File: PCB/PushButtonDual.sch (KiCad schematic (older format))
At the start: 3 parts, among them SW3 PCB_Push_Button, SW4 PCB_Push_Button

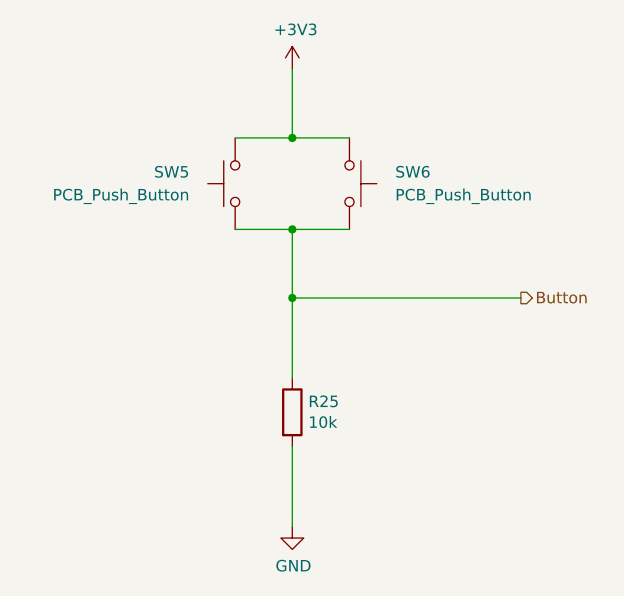
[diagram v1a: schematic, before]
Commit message: Improve the push buttons
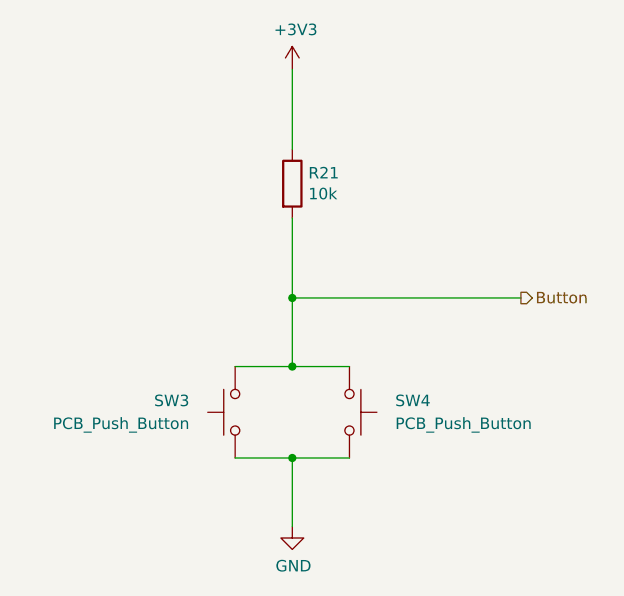
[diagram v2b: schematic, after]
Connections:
- net +3V3: now also R21.1; no longer SW3.1, SW4.1
- net Button: now also R21.2, SW3.1, SW4.1; no longer R21.1, SW3.2, SW4.2
- net GND: now also SW3.2, SW4.2; no longer R21.2
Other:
- moved on the sheet: R21, SW3, SW4
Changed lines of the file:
@@
 $Descr A4 11693 8268
 encoding utf-8
-Sheet 13 19
+Sheet 11 19
 Title "Litter Robot 3 - Push button (dual)"
 Date "2021-03-28"
@@
 L Device:R R?
 U 1 1 604E1842
-P 5000 4000
+P 5000 3000
 AR Path="/603F20AB/604E1842" Ref="R?"  Part="1"
 AR Path="/603F1DCE/604E1842" Ref="R?"  Part="1"
@@
 AR Path="/603F1F4D/605BE155/604E1842" Ref="R?"  Part="1"
 AR Path="/603F1F4D/605BE15D/604E1842" Ref="R?"  Part="1"
-F 0 "R25" H 5070 4046 50  0000 L CNN
-F 1 "10k" H 5070 3955 50  0000 L CNN
-F 2 "Resistor_SMD:R_0603_1608Metric" V 4930 4000 50  0001 C CNN
-F 3 "https://www.bourns.com/docs/product-datasheets/CRxxxxx.pdf" H 5000 4000 50  0001 C CNN
-F 4 "CR0603-FX-1002ELF" H 5000 4000 50  0001 C CNN "Part_number"
-	1    5000 4000
+F 0 "R21" H 5070 3046 50  0000 L CNN
+F 1 "10k" H 5070 2955 50  0000 L CNN
+F 2 "Resistor_SMD:R_0603_1608Metric" V 4930 3000 50  0001 C CNN
+F 3 "https://www.bourns.com/docs/product-datasheets/CRxxxxx.pdf" H 5000 3000 50  0001 C CNN
+F 4 "CR0603-FX-1002ELF" H 5000 3000 50  0001 C CNN "Part_number"
+	1    5000 3000
 	1    0    0    -1
 $EndComp
@@
 AR Path="/603F1F4D/605BE155/604E1848" Ref="#PWR?"  Part="1"
 AR Path="/603F1F4D/605BE15D/604E1848" Ref="#PWR?"  Part="1"
-F 0 "#PWR046" H 5000 2350 50  0001 C CNN
+F 0 "#PWR040" H 5000 2350 50  0001 C CNN
 F 1 "+3V3" H 5015 2673 50  0000 C CNN
 F 2 "" H 5000 2500 50  0001 C CNN
@@
 AR Path="/603F1F4D/605BE155/604E184E" Ref="#PWR?"  Part="1"
 AR Path="/603F1F4D/605BE15D/604E184E" Ref="#PWR?"  Part="1"
-F 0 "#PWR047" H 5000 4250 50  0001 C CNN
+F 0 "#PWR041" H 5000 4250 50  0001 C CNN
 F 1 "GND" H 5005 4327 50  0000 C CNN
 F 2 "" H 5000 4500 50  0001 C CNN
@@
 $EndComp
 Wire Wire Line
-	5000 2500 5000 2800
+	5000 3500 5000 3800
 Wire Wire Line
-	5000 3200 5000 3500
-Wire Wire Line
-	5000 4150 5000 4500
+	5000 4200 5000 4500
 Wire Wire Line
 	6000 3500 5000 3500
-Connection ~ 5000 3500
-Wire Wire Line
-	5000 3500 5000 3850
 Text HLabel 6000 3500 2    50   Output ~ 0
 Button
 Wire Wire Line
-	4750 2800 5000 2800
-Connection ~ 5000 2800
+	4750 3800 5000 3800
+Connection ~ 5000 3800
 Wire Wire Line
-	5000 2800 5250 2800
+	5000 3800 5250 3800
 Wire Wire Line
-	4750 3200 5000 3200
-Connection ~ 5000 3200
+	4750 4200 5000 4200
+Connection ~ 5000 4200
 Wire Wire Line
-	5000 3200 5250 3200
+	5000 4200 5250 4200
 $Comp
 L Switch:SW_Push SW?
 U 1 1 604E185B
-P 5250 3000
+P 5250 4000
 AR Path="/603E03AA/603C09F0/604E185B" Ref="SW?"  Part="1"
 AR Path="/603E03AA/603C05C6/604E185B" Ref="SW?"  Part="1"
@@
 AR Path="/603F1F4D/605BE155/604E185B" Ref="SW?"  Part="1"
 AR Path="/603F1F4D/605BE15D/604E185B" Ref="SW?"  Part="1"
-F 0 "SW6" V 5200 3200 50  0000 L CNN
-F 1 "PCB_Push_Button" V 5300 3200 50  0000 L CNN
-F 2 "LitterRobot:PCB_Push_Button_5mm_0.4mm" H 5250 3200 50  0001 C CNN
-F 3 "~" H 5250 3200 50  0001 C CNN
-	1    5250 3000
+F 0 "SW4" V 5200 4200 50  0000 L CNN
+F 1 "PCB_Push_Button" V 5300 4200 50  0000 L CNN
+F 2 "LitterRobot:PCB_Push_Button_5mm_0.4mm" H 5250 4200 50  0001 C CNN
+F 3 "~" H 5250 4200 50  0001 C CNN
+	1    5250 4000
 	0    1    1    0
 $EndComp
@@
 L Switch:SW_Push SW?
 U 1 1 604E42E5
-P 4750 3000
+P 4750 4000
 AR Path="/603E03AA/603C09F0/604E42E5" Ref="SW?"  Part="1"
 AR Path="/603E03AA/603C05C6/604E42E5" Ref="SW?"  Part="1"
@@
 AR Path="/603F1F4D/605BE155/604E42E5" Ref="SW?"  Part="1"
 AR Path="/603F1F4D/605BE15D/604E42E5" Ref="SW?"  Part="1"
-F 0 "SW5" V 4700 3200 50  0000 L CNN
-F 1 "PCB_Push_Button" V 4800 3200 50  0000 L CNN
-F 2 "LitterRobot:PCB_Push_Button_5mm_0.4mm" H 4750 3200 50  0001 C CNN
-F 3 "~" H 4750 3200 50  0001 C CNN
-	1    4750 3000
+F 0 "SW3" V 4700 4200 50  0000 L CNN
+F 1 "PCB_Push_Button" V 4800 4200 50  0000 L CNN
+F 2 "LitterRobot:PCB_Push_Button_5mm_0.4mm" H 4750 4200 50  0001 C CNN
+F 3 "~" H 4750 4200 50  0001 C CNN
+	1    4750 4000
 	0    -1   1    0
 $EndComp
+Wire Wire Line
+	5000 3150 5000 3500
+Wire Wire Line
+	5000 2500 5000 2850
+Connection ~ 5000 3500
 $EndSCHEMATC

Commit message: Add reverse polarity protection diodes
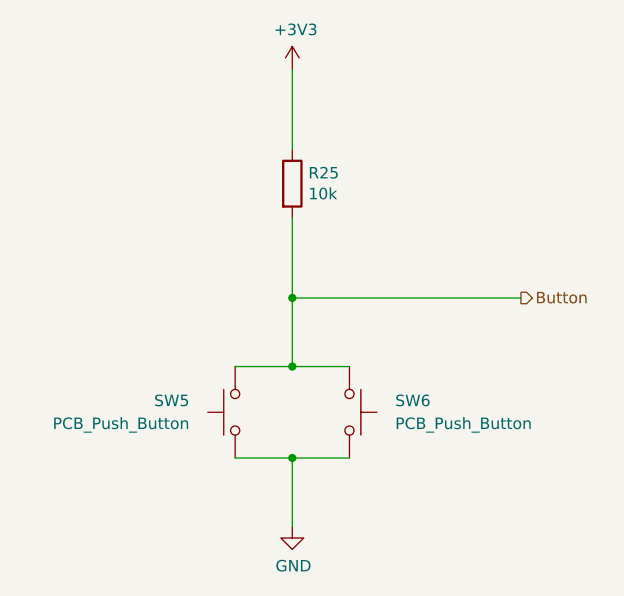
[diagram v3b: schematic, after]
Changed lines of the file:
@@
 AR Path="/603F1F4D/605BE155/604E1842" Ref="R?"  Part="1"
 AR Path="/603F1F4D/605BE15D/604E1842" Ref="R?"  Part="1"
-F 0 "R21" H 5070 3046 50  0000 L CNN
+F 0 "R25" H 5070 3046 50  0000 L CNN
 F 1 "10k" H 5070 2955 50  0000 L CNN
 F 2 "Resistor_SMD:R_0603_1608Metric" V 4930 3000 50  0001 C CNN
@@
 AR Path="/603F1F4D/605BE155/604E1848" Ref="#PWR?"  Part="1"
 AR Path="/603F1F4D/605BE15D/604E1848" Ref="#PWR?"  Part="1"
-F 0 "#PWR040" H 5000 2350 50  0001 C CNN
+F 0 "#PWR046" H 5000 2350 50  0001 C CNN
 F 1 "+3V3" H 5015 2673 50  0000 C CNN
 F 2 "" H 5000 2500 50  0001 C CNN
@@
 AR Path="/603F1F4D/605BE155/604E184E" Ref="#PWR?"  Part="1"
 AR Path="/603F1F4D/605BE15D/604E184E" Ref="#PWR?"  Part="1"
-F 0 "#PWR041" H 5000 4250 50  0001 C CNN
+F 0 "#PWR047" H 5000 4250 50  0001 C CNN
 F 1 "GND" H 5005 4327 50  0000 C CNN
 F 2 "" H 5000 4500 50  0001 C CNN
@@
 AR Path="/603F1F4D/605BE155/604E185B" Ref="SW?"  Part="1"
 AR Path="/603F1F4D/605BE15D/604E185B" Ref="SW?"  Part="1"
-F 0 "SW4" V 5200 4200 50  0000 L CNN
+F 0 "SW6" V 5200 4200 50  0000 L CNN
 F 1 "PCB_Push_Button" V 5300 4200 50  0000 L CNN
 F 2 "LitterRobot:PCB_Push_Button_5mm_0.4mm" H 5250 4200 50  0001 C CNN
@@
 AR Path="/603F1F4D/605BE155/604E42E5" Ref="SW?"  Part="1"
 AR Path="/603F1F4D/605BE15D/604E42E5" Ref="SW?"  Part="1"
-F 0 "SW3" V 4700 4200 50  0000 L CNN
+F 0 "SW5" V 4700 4200 50  0000 L CNN
 F 1 "PCB_Push_Button" V 4800 4200 50  0000 L CNN
 F 2 "LitterRobot:PCB_Push_Button_5mm_0.4mm" H 4750 4200 50  0001 C CNN

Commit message: Add support for the weight sensor
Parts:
- renumbered R21 to R23
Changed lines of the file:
@@
 $Descr A4 11693 8268
 encoding utf-8
-Sheet 11 19
+Sheet 11 20
 Title "Litter Robot 3 - Push button (dual)"
-Date "2021-03-28"
+Date "2021-04-02"
 Rev "A1"
 Comp "L. Sartory"
@@
 AR Path="/603E03AA/603C06CF/604E1842" Ref="R?"  Part="1"
 AR Path="/603E03AA/603C09F0/604E1842" Ref="R?"  Part="1"
-AR Path="/603E03AA/604DE92D/604E1842" Ref="R21"  Part="1"
-AR Path="/603E03AA/604E2A9A/604E1842" Ref="R25"  Part="1"
+AR Path="/603E03AA/604DE92D/604E1842" Ref="R23"  Part="1"
+AR Path="/603E03AA/604E2A9A/604E1842" Ref="R27"  Part="1"
 AR Path="/603F1F4D/605BE155/604E1842" Ref="R?"  Part="1"
 AR Path="/603F1F4D/605BE15D/604E1842" Ref="R?"  Part="1"
-F 0 "R25" H 5070 3046 50  0000 L CNN
+F 0 "R27" H 5070 3046 50  0000 L CNN
 F 1 "10k" H 5070 2955 50  0000 L CNN
 F 2 "Resistor_SMD:R_0603_1608Metric" V 4930 3000 50  0001 C CNN
@@
 AR Path="/603E03AA/603C06CF/604E1848" Ref="#PWR?"  Part="1"
 AR Path="/603E03AA/603C09F0/604E1848" Ref="#PWR?"  Part="1"
-AR Path="/603E03AA/604DE92D/604E1848" Ref="#PWR040"  Part="1"
-AR Path="/603E03AA/604E2A9A/604E1848" Ref="#PWR046"  Part="1"
+AR Path="/603E03AA/604DE92D/604E1848" Ref="#PWR041"  Part="1"
+AR Path="/603E03AA/604E2A9A/604E1848" Ref="#PWR047"  Part="1"
 AR Path="/603F1F4D/605BE155/604E1848" Ref="#PWR?"  Part="1"
 AR Path="/603F1F4D/605BE15D/604E1848" Ref="#PWR?"  Part="1"
-F 0 "#PWR046" H 5000 2350 50  0001 C CNN
+F 0 "#PWR047" H 5000 2350 50  0001 C CNN
 F 1 "+3V3" H 5015 2673 50  0000 C CNN
 F 2 "" H 5000 2500 50  0001 C CNN
@@
 AR Path="/603E03AA/603C06CF/604E184E" Ref="#PWR?"  Part="1"
 AR Path="/603E03AA/603C09F0/604E184E" Ref="#PWR?"  Part="1"
-AR Path="/603E03AA/604DE92D/604E184E" Ref="#PWR041"  Part="1"
-AR Path="/603E03AA/604E2A9A/604E184E" Ref="#PWR047"  Part="1"
+AR Path="/603E03AA/604DE92D/604E184E" Ref="#PWR042"  Part="1"
+AR Path="/603E03AA/604E2A9A/604E184E" Ref="#PWR048"  Part="1"
 AR Path="/603F1F4D/605BE155/604E184E" Ref="#PWR?"  Part="1"
 AR Path="/603F1F4D/605BE15D/604E184E" Ref="#PWR?"  Part="1"
-F 0 "#PWR047" H 5000 4250 50  0001 C CNN
+F 0 "#PWR048" H 5000 4250 50  0001 C CNN
 F 1 "GND" H 5005 4327 50  0000 C CNN
 F 2 "" H 5000 4500 50  0001 C CNN

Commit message: Re-annotate all components
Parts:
- renumbered R23 to R33, SW3 to SW2, SW4 to SW3
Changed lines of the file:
@@
 $Descr A4 11693 8268
 encoding utf-8
-Sheet 11 22
+Sheet 15 22
 Title "Litter Robot 3 - Push button (dual)"
-Date "2021-04-03"
+Date "2021-04-05"
 Rev "A1"
 Comp "L. Sartory"
@@
 AR Path="/603E03AA/603C06CF/604E1842" Ref="R?"  Part="1"
 AR Path="/603E03AA/603C09F0/604E1842" Ref="R?"  Part="1"
-AR Path="/603E03AA/604DE92D/604E1842" Ref="R23"  Part="1"
-AR Path="/603E03AA/604E2A9A/604E1842" Ref="R27"  Part="1"
+AR Path="/603E03AA/604DE92D/604E1842" Ref="R33"  Part="1"
+AR Path="/603E03AA/604E2A9A/604E1842" Ref="R35"  Part="1"
 AR Path="/603F1F4D/605BE155/604E1842" Ref="R?"  Part="1"
 AR Path="/603F1F4D/605BE15D/604E1842" Ref="R?"  Part="1"
-F 0 "R27" H 5070 3046 50  0000 L CNN
+F 0 "R35" H 5070 3046 50  0000 L CNN
 F 1 "10k" H 5070 2955 50  0000 L CNN
 F 2 "Resistor_SMD:R_0603_1608Metric" V 4930 3000 50  0001 C CNN
@@
 AR Path="/603E03AA/603C06CF/604E1848" Ref="#PWR?"  Part="1"
 AR Path="/603E03AA/603C09F0/604E1848" Ref="#PWR?"  Part="1"
-AR Path="/603E03AA/604DE92D/604E1848" Ref="#PWR041"  Part="1"
-AR Path="/603E03AA/604E2A9A/604E1848" Ref="#PWR047"  Part="1"
+AR Path="/603E03AA/604DE92D/604E1848" Ref="#PWR086"  Part="1"
+AR Path="/603E03AA/604E2A9A/604E1848" Ref="#PWR090"  Part="1"
 AR Path="/603F1F4D/605BE155/604E1848" Ref="#PWR?"  Part="1"
 AR Path="/603F1F4D/605BE15D/604E1848" Ref="#PWR?"  Part="1"
-F 0 "#PWR047" H 5000 2350 50  0001 C CNN
+F 0 "#PWR090" H 5000 2350 50  0001 C CNN
 F 1 "+3V3" H 5015 2673 50  0000 C CNN
 F 2 "" H 5000 2500 50  0001 C CNN
@@
 AR Path="/603E03AA/603C06CF/604E184E" Ref="#PWR?"  Part="1"
 AR Path="/603E03AA/603C09F0/604E184E" Ref="#PWR?"  Part="1"
-AR Path="/603E03AA/604DE92D/604E184E" Ref="#PWR042"  Part="1"
-AR Path="/603E03AA/604E2A9A/604E184E" Ref="#PWR048"  Part="1"
+AR Path="/603E03AA/604DE92D/604E184E" Ref="#PWR087"  Part="1"
+AR Path="/603E03AA/604E2A9A/604E184E" Ref="#PWR091"  Part="1"
 AR Path="/603F1F4D/605BE155/604E184E" Ref="#PWR?"  Part="1"
 AR Path="/603F1F4D/605BE15D/604E184E" Ref="#PWR?"  Part="1"
-F 0 "#PWR048" H 5000 4250 50  0001 C CNN
+F 0 "#PWR091" H 5000 4250 50  0001 C CNN
 F 1 "GND" H 5005 4327 50  0000 C CNN
 F 2 "" H 5000 4500 50  0001 C CNN
@@
 AR Path="/603E03AA/603C0699/604E185B" Ref="SW?"  Part="1"
 AR Path="/603E03AA/603C06CF/604E185B" Ref="SW?"  Part="1"
-AR Path="/603E03AA/604DE92D/604E185B" Ref="SW4"  Part="1"
+AR Path="/603E03AA/604DE92D/604E185B" Ref="SW3"  Part="1"
 AR Path="/603E03AA/604E2A9A/604E185B" Ref="SW6"  Part="1"
 AR Path="/603F1F4D/605BE155/604E185B" Ref="SW?"  Part="1"
@@
 AR Path="/603E03AA/603C0699/604E42E5" Ref="SW?"  Part="1"
 AR Path="/603E03AA/603C06CF/604E42E5" Ref="SW?"  Part="1"
-AR Path="/603E03AA/604DE92D/604E42E5" Ref="SW3"  Part="1"
+AR Path="/603E03AA/604DE92D/604E42E5" Ref="SW2"  Part="1"
 AR Path="/603E03AA/604E2A9A/604E42E5" Ref="SW5"  Part="1"
 AR Path="/603F1F4D/605BE155/604E42E5" Ref="SW?"  Part="1"
